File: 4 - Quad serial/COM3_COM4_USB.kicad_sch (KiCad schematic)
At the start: 15 parts

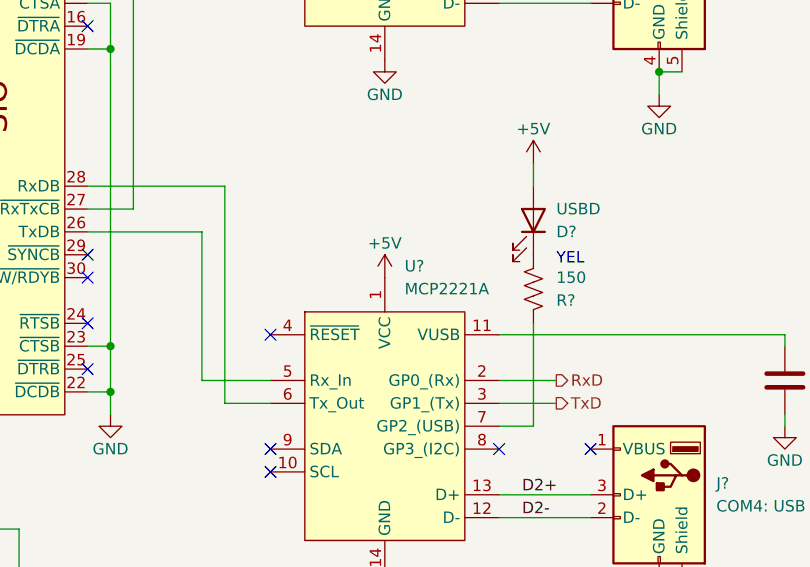
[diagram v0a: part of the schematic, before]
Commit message: Made a mess of things a bit.
Software clock is non-functional. Worked on the breadboard, but makes the CPU board crash when writing to the IO port to select clock speed.
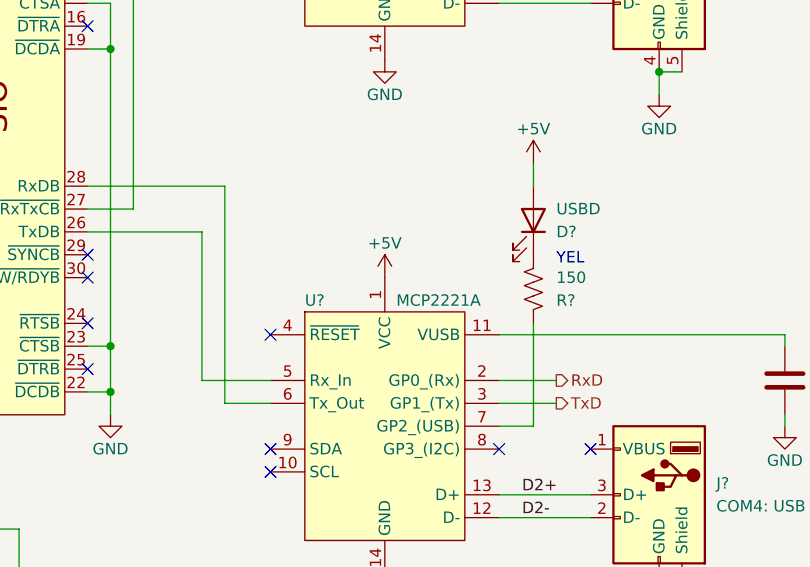
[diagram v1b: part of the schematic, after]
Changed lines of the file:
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@@
   )
   (symbol (lib_id "0_Library:MCP2221A") (at 138.43 111.76 0) (unit 1)
-    (in_bom yes) (on_board yes) (dnp no) (fields_autoplaced)
-    (property "Reference" "U?" (at 140.6241 106.68 0)
+    (in_bom yes) (on_board yes) (dnp no)
+    (property "Reference" "U?" (at 129.54 110.49 0)
       (effects (font (size 1.27 1.27)) (justify left))
     )
-    (property "Value" "MCP2221A" (at 140.6241 109.22 0)
+    (property "Value" "MCP2221A" (at 139.7 110.49 0)
       (effects (font (size 1.27 1.27)) (justify left))
     )

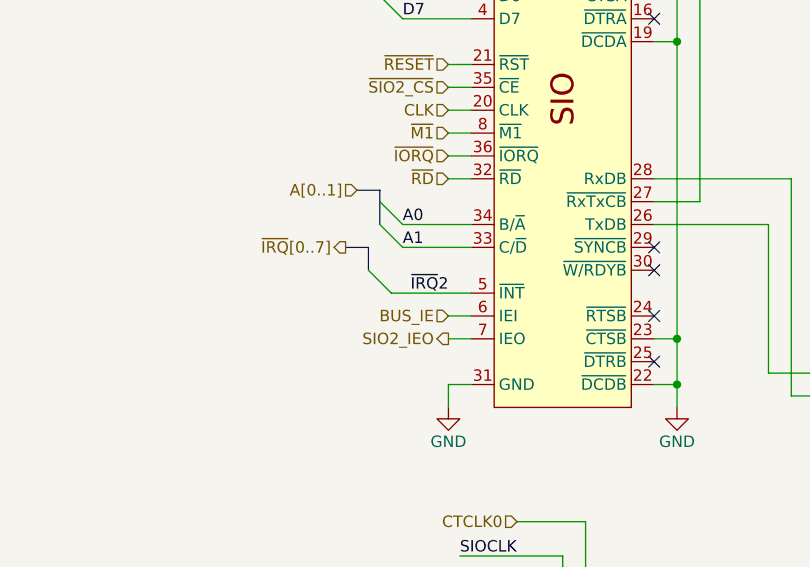
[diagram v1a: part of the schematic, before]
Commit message: Rerouted some traces and readied the the gerber to send out to manufacturing
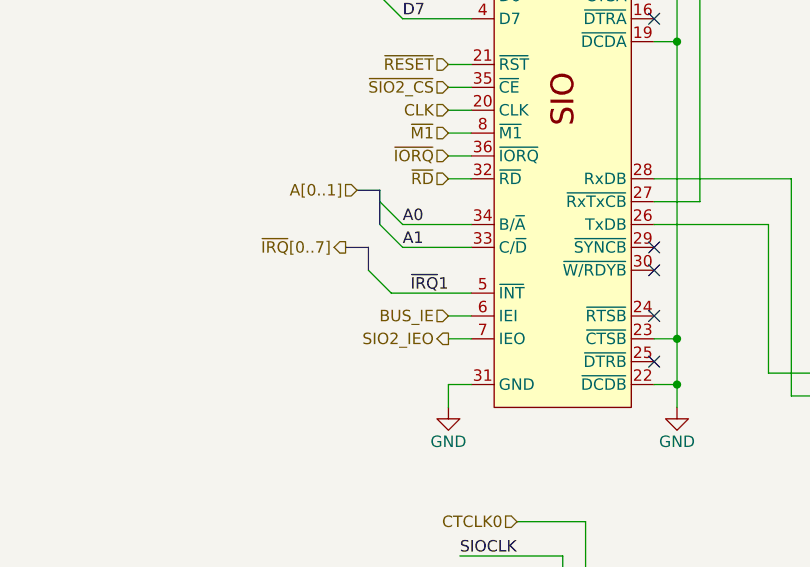
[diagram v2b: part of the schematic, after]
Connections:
- net ~{IRQ}2 renamed ~{IRQ}1
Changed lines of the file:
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@@
     (effects (font (size 1.27 1.27)) (justify left bottom))
   )
-  (label "~{IRQ}2" (at 82.55 110.49 180) (fields_autoplaced)
+  (label "~{IRQ}1" (at 82.55 110.49 180) (fields_autoplaced)
     (effects (font (size 1.27 1.27)) (justify right bottom))
   )
